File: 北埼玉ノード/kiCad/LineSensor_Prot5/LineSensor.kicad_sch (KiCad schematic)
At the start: 113 parts, among them J1 Conn_01x04_Socket, J2 Conn_01x02_Socket, Q1 Q_Photo_NPN, Q10 Q_Photo_NPN, Q11 Q_Photo_NPN, Q12 Q_Photo_NPN, Q13 Q_Photo_NPN, Q14 Q_Photo_NPN, Q15 Q_Photo_NPN, Q16 Q_Photo_NPN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

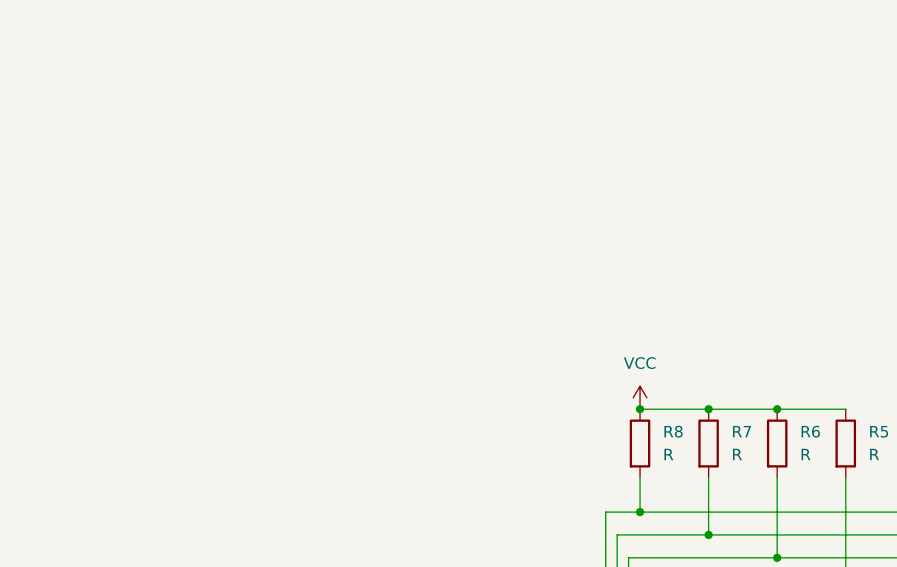
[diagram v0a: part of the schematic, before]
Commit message: ラインセンサー部品ほぼ決定
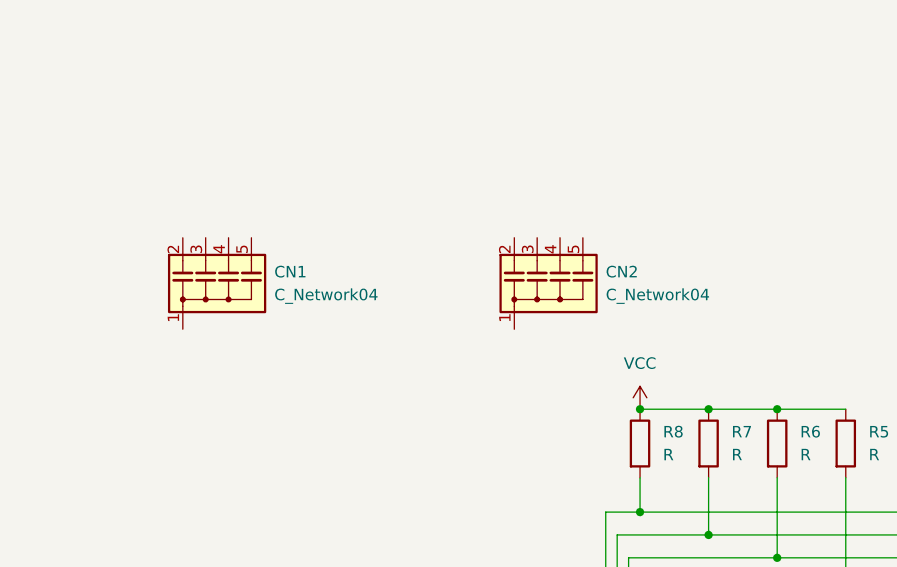
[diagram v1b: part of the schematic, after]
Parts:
- added CN1, CN2: C_Network04, symbol Device:C_Network04
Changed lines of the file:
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@@
 	)
 	(symbol
+		(lib_id "Device:C_Network04")
+		(at 358.14 387.35 0)
+		(unit 1)
+		(exclude_from_sim no)
+		(in_bom yes)
+		(on_board yes)
+		(dnp no)
+		(fields_autoplaced yes)
+		(property "Reference" "CN1"
+			(at 363.22 386.0799 0)
+			(effects
+				(font
+					(size 1.27 1.27)
+				)
+				(justify left)
+			)
+		)
+		(property "Value" "C_Network04"
+			(at 363.22 388.6199 0)
+			(effects
+				(font
+					(size 1.27 1.27)
+				)
+				(justify left)
+			)
+		)
+		(property "Footprint" ""
+			(at 365.252 387.35 90)
+			(effects
+				(font
+					(size 1.27 1.27)
+				)
+				(hide yes)
+			)
+		)
+		(property "Datasheet" "~"
+			(at 355.6 387.35 0)
+			(effects
+				(font
+					(size 1.27 1.27)
+				)
+				(hide yes)
+			)
+		)
+		(property "Description" "4 capacitor network, star topology, bussed capacitors, single bus pin, small symbol, SIP-5"
+			(at 358.14 387.35 0)
+			(effects
+				(font
+					(size 1.27 1.27)
+				)
+				(hide yes)
+			)
+		)
+		(pin "1"
+		)
+		(pin "4"
+		)
+		(pin "3"
+		)
+		(pin "2"
+		)
+		(pin "5"
+		)
+		(instances
+			(project ""
+				(path "/acb76ddc-37df-49ad-a534-a7b141941dd0"
+					(reference "CN1")
+					(unit 1)
+				)
+			)
+		)
+	)
+	(symbol
 		(lib_id "power:GND")
 		(at 612.14 196.85 0)
@@
 					(unit 1)
 				)
+			)
+		)
+	)
+	(symbol
+		(lib_id "Device:C_Network04")
+		(at 394.97 387.35 0)
+		(unit 1)
+		(exclude_from_sim no)
+		(in_bom yes)
+		(on_board yes)
+		(dnp no)
+		(fields_autoplaced yes)
+		(property "Reference" "CN2"
+			(at 400.05 386.0799 0)
+			(effects
+				(font
+					(size 1.27 1.27)
+				)
+				(justify left)
+			)
+		)
+		(property "Value" "C_Network04"
+			(at 400.05 388.6199 0)
+			(effects
+				(font
+					(size 1.27 1.27)
+				)
+				(justify left)
+			)
+		)
+		(property "Footprint" ""
+			(at 402.082 387.35 90)
+			(effects
+				(font
+					(size 1.27 1.27)
+				)
+				(hide yes)
+			)
+		)
+		(property "Datasheet" "~"
+			(at 392.43 387.35 0)
+			(effects
+				(font
+					(size 1.27 1.27)
+				)
+				(hide yes)
+			)
+		)
+		(property "Description" "4 capacitor network, star topology, bussed capacitors, single bus pin, small symbol, SIP-5"
+			(at 394.97 387.35 0)
+			(effects
+				(font
+					(size 1.27 1.27)
+				)
+				(hide yes)
+			)
+		)
+		(pin "5"
+		)
+		(pin "3"
+		)
+		(pin "2"
+		)
+		(pin "4"
+		)
+		(pin "1"
+		)
+		(instances
+			(project ""
+				(path "/acb76ddc-37df-49ad-a534-a7b141941dd0"
+					(reference "CN2")
+					(unit 1)
+				)
